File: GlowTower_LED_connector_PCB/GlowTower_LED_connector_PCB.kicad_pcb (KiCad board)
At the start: 2 copper layers, 28.6 x 28.6 mm, 0 parts

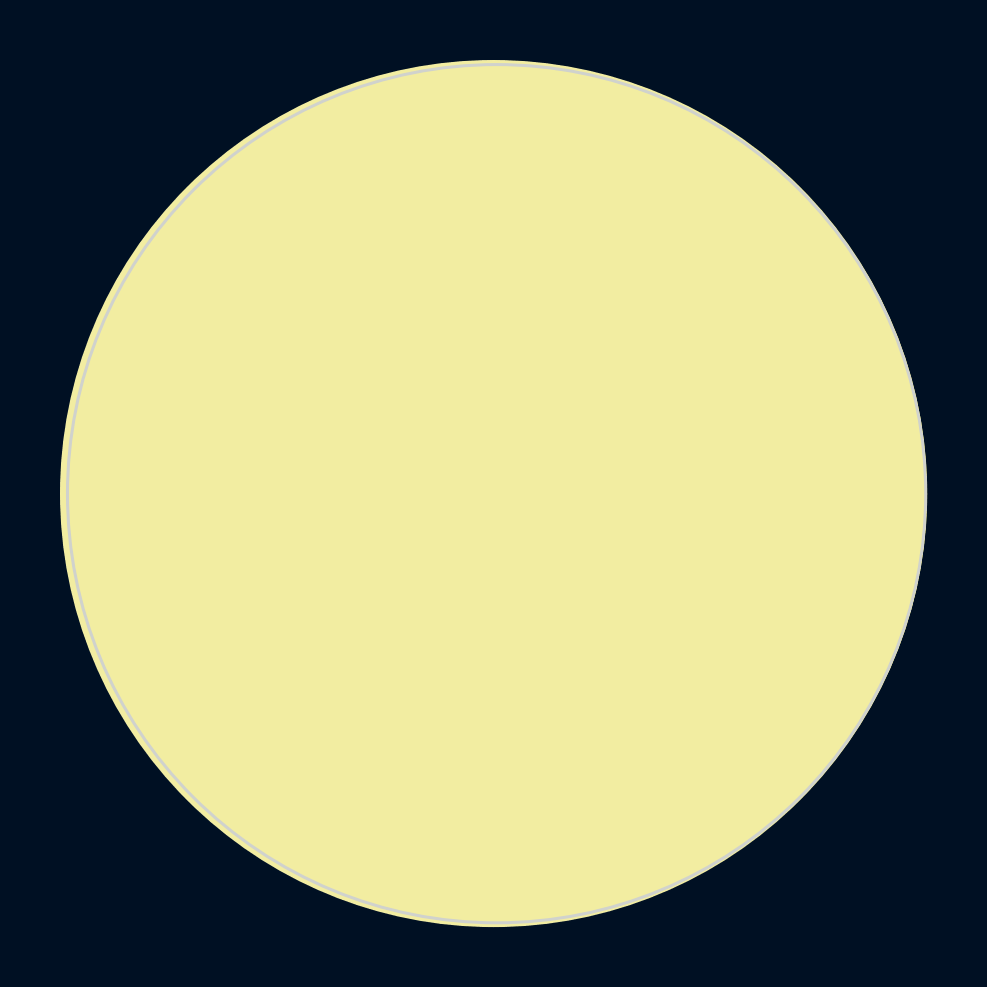
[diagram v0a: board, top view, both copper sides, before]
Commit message: update screenshots of PCBs
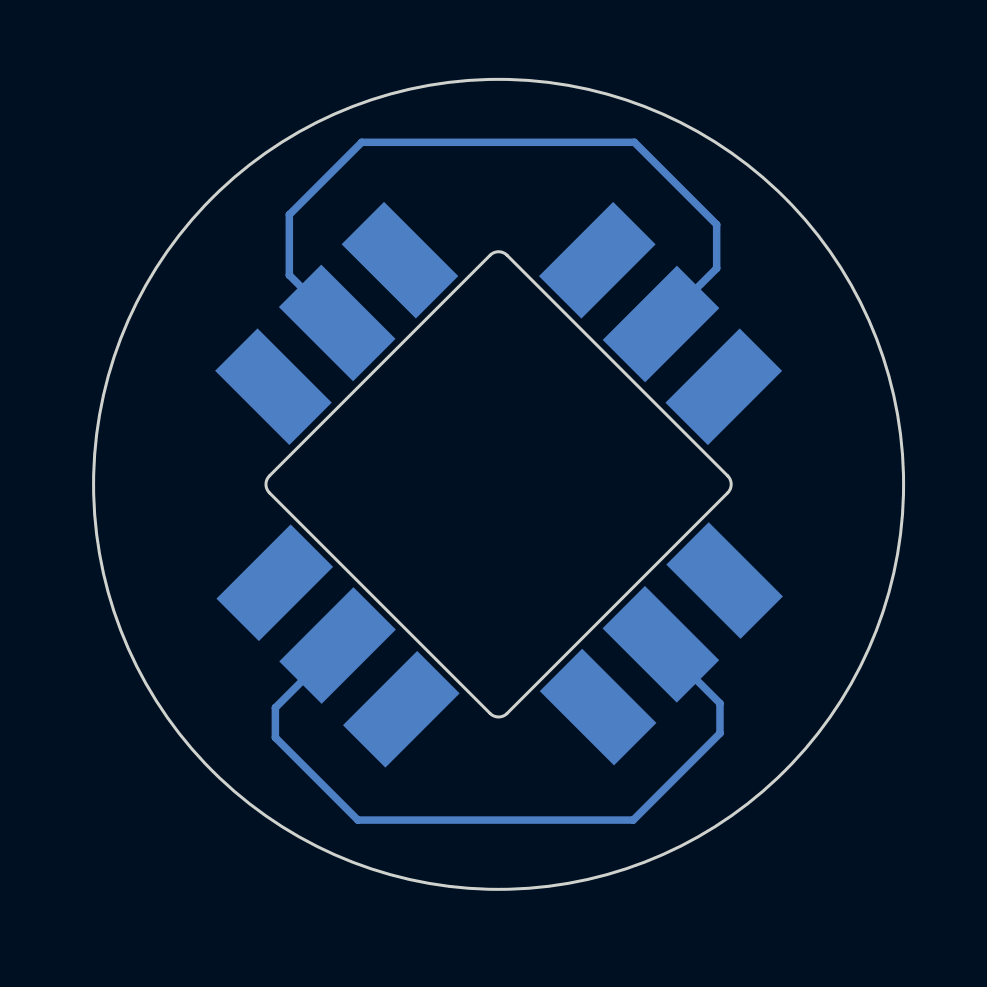
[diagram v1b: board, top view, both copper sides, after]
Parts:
- added U1: LED strip, Connector:LED strip connector pad, B.Cu at (107.3, 77.8)
- added U2: LED strip, Connector:LED strip connector pad, B.Cu at (95.9, 66.6)
- added U3: LED strip, Connector:LED strip connector pad, B.Cu at (96.0, 77.9)
- added U4: LED strip, Connector:LED strip connector pad, B.Cu at (107.2, 66.6)
- added leddirectionarrow1: LOGO, LOGO, B.Cu at (109.6, 64.5)
- added leddirectionarrow2: LOGO, LOGO, B.Cu at (93.9, 64.5)
- added leddirectionarrow3: LOGO, LOGO, B.Cu at (94.0, 80.1)
- added leddirectionarrow4: LOGO, LOGO, B.Cu at (109.4, 79.9)
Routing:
- net (no net): track 51.9 -> 0.00 mm
- net Net-(U1-Pad2): track 0.00 -> 24.9 mm
- net Net-(U2-Pad2): track 0.00 -> 24.7 mm
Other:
- board size 28.6 x 28.6 mm -> 27 x 27 mm

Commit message: updated pcb design (in progress)
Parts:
- added SW1: TS-1102S-C-A-B, TS-1102S-C-A-B:TS-1102S-C-A-B, F.Cu at (101.4, 72.4)
- U1, U2, U3, U4: footprint Connector:LED strip connector pad -> myparts:LED strip connector 4pad supersmall
- moved leddirectionarrow1 8.40 mm to (101.5, 66.7)
- moved leddirectionarrow4 8.22 mm to (107.2, 72.0)
- moved leddirectionarrow2 8.12 mm to (96.2, 72.3)
- moved leddirectionarrow3 8.04 mm to (101.7, 77.8)
- moved U3 1.16 mm to (96.8, 77.0)
- moved U1 1.14 mm to (106.5, 77.0)
- moved U2 1.12 mm to (96.8, 67.3)
- moved U4 1.10 mm to (106.4, 67.3)
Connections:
- U1 pad 1: unconnected-(U1-Pad1) -> BUTTON
- U1 pad 2: Net-(U1-Pad2) -> GND
- U1 pad 3: unconnected-(U1-Pad3) -> Net-(U1-Pad3)
- U2 pad 2: Net-(U2-Pad2) -> unconnected-(U2-Pad2)
- U2 pad 3: unconnected-(U2-Pad3) -> Net-(U2-Pad3)
- U3 pad 2: Net-(U1-Pad2) -> Net-(U1-Pad3)
- U4 pad 2: Net-(U2-Pad2) -> Net-(U2-Pad3)
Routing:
- net Net-(U1-Pad2): track 24.9 -> 0.00 mm
- net Net-(U2-Pad2): track 24.7 -> 0.00 mm
- net BUTTON: track 0.00 -> 14.2 mm, vias 0 -> 1
- net GND: track 0.00 -> 11.3 mm, vias 0 -> 1
- net Net-(U1-Pad3): track 0.00 -> 9.61 mm
- net Net-(U2-Pad3): track 0.00 -> 9.38 mm
- added copper zone on B.Cu, net GND
- added copper zone on F.Cu, net GND
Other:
- board size 27 x 27 mm -> 20.1 x 20.1 mm
- board text added: "GlowTower /GlowLight"
- board text added: "LED connector beta 2"

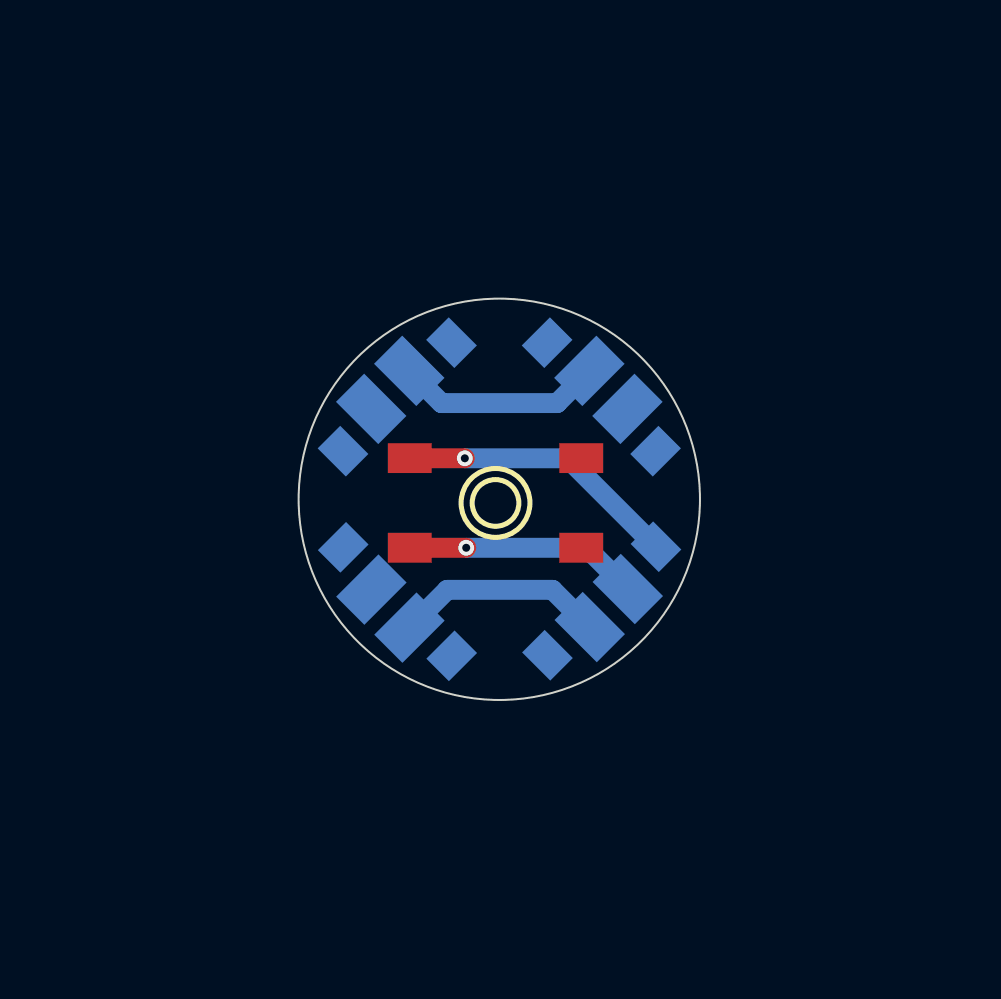
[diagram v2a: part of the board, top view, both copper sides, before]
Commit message: redesigned GlowTower/GlowLight main pcb
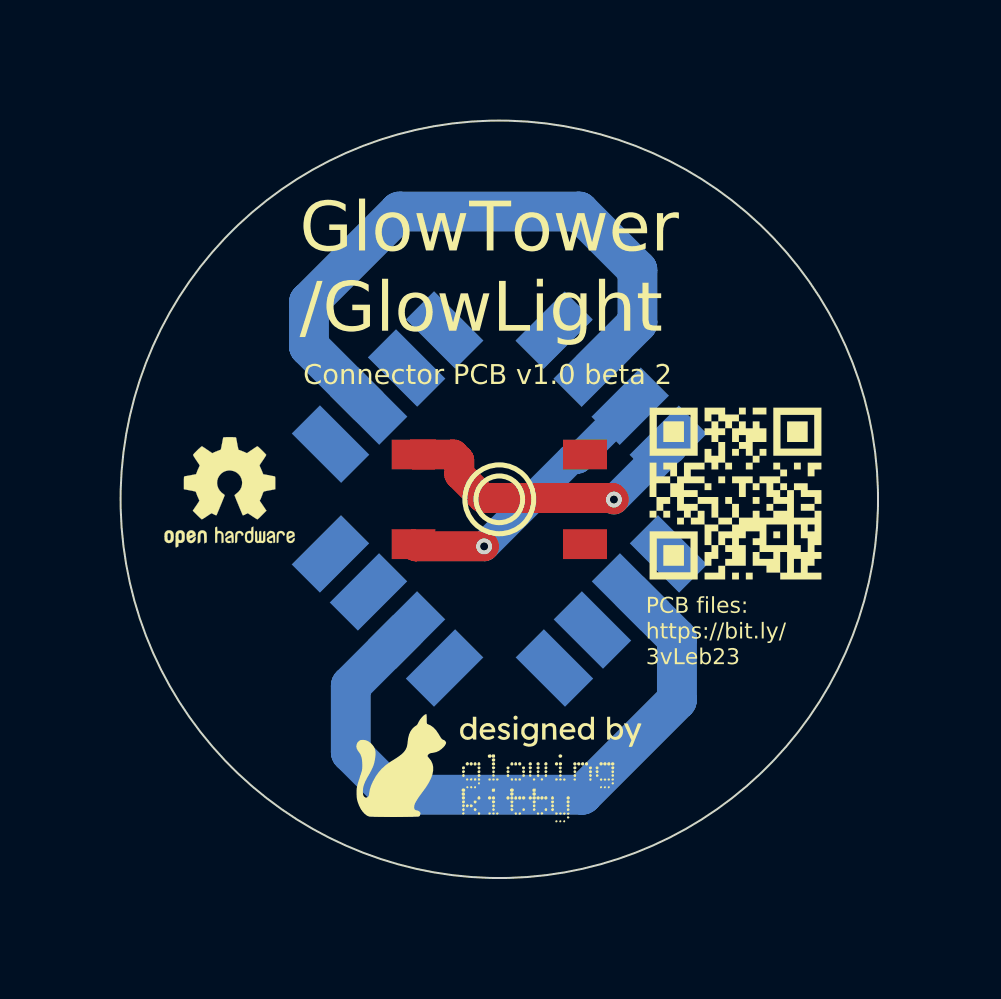
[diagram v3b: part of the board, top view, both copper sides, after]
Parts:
- added OSHW logo: OSHW-Logo2_7.3x6mm_SilkScreen, Symbol:OSHW-Logo2_7.3x6mm_SilkScreen, F.Cu at (88.1, 71.8)
- added designedby: LOGO, LOGO, F.Cu at (101.6, 85.6)
- added qrcode: LOGO, LOGO, F.Cu at (113.5, 71.9)
- U1: renamed from U4; footprint myparts:LED strip connector 4pad supersmall -> myparts:LED strip connector 4pad
- U2: renamed from U3; footprint myparts:LED strip connector 4pad supersmall -> myparts:LED strip connector 4pad
- U3: renamed from U2; footprint myparts:LED strip connector 4pad supersmall -> myparts:LED strip connector 4pad
- U4: renamed from U1; footprint myparts:LED strip connector 4pad supersmall -> myparts:LED strip connector 4pad
- moved leddirectionarrow1 16.2 mm to (111.0, 79.7), turned to 45 degrees
- moved leddirectionarrow4 9.72 mm to (109.3, 62.5), turned to -45 degrees
- moved leddirectionarrow2 9.15 mm to (91.8, 64.2), turned to -135 degrees
- moved leddirectionarrow3 8.52 mm to (94.1, 81.5), turned to 135 degrees
- moved U4 1.45 mm to (107.5, 78.0)
- moved U3 1.44 mm to (95.7, 66.3)
- moved U1 1.44 mm to (107.5, 66.3)
- moved U2 1.44 mm to (95.8, 78.0)
- moved SW1 0.26 mm to (101.6, 72.2)
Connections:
- U1 pad 2: Net-(U2-Pad3) -> Net-(U3-Pad2)
- U1 pad 3: unconnected-(U4-Pad3) -> GND
- U1 pad 4: unconnected-(U4-Pad4) (its old number) -> BUTTON
- U2 pad 2: Net-(U1-Pad3) -> Net-(U4-Pad2)
- U3 pad 2: unconnected-(U2-Pad2) -> Net-(U3-Pad2)
- U3 pad 3: Net-(U2-Pad3) -> unconnected-(U3-Pad3)
- U4 pad 1: BUTTON -> unconnected-(U4-Pad1)
- U4 pad 2: GND -> Net-(U4-Pad2)
- U4 pad 3: Net-(U1-Pad3) -> unconnected-(U4-Pad3)
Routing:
- net Net-(U4-Pad2): track 0.00 -> 32.9 mm
- net Net-(U3-Pad2): track 0.00 -> 31.9 mm
- net Net-(U1-Pad3): track 9.61 -> 0.00 mm
- net Net-(U2-Pad3): track 9.38 -> 0.00 mm
- net GND: track 11.3 -> 13.8 mm
- net BUTTON: track 14.2 -> 15.3 mm
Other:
- board size 20.1 x 20.1 mm -> 38 x 38 mm
- board text added: "Connector PCB v1.0 beta 2"
- board text added: "PCB files: https://bit.ly/ 3vLeb23"
- board text removed: "LED connector beta 2"
